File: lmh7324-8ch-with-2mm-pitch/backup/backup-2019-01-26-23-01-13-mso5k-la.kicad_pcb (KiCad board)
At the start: 4 copper layers, 40 x 44 mm, 101 parts, among them IC201 lmh7324, IC401 lmh7324, J101 out, J102 in, J103 3mm, J104 3mm, J105 3mm, J106 3mm, U401 ATtiny85-20SU

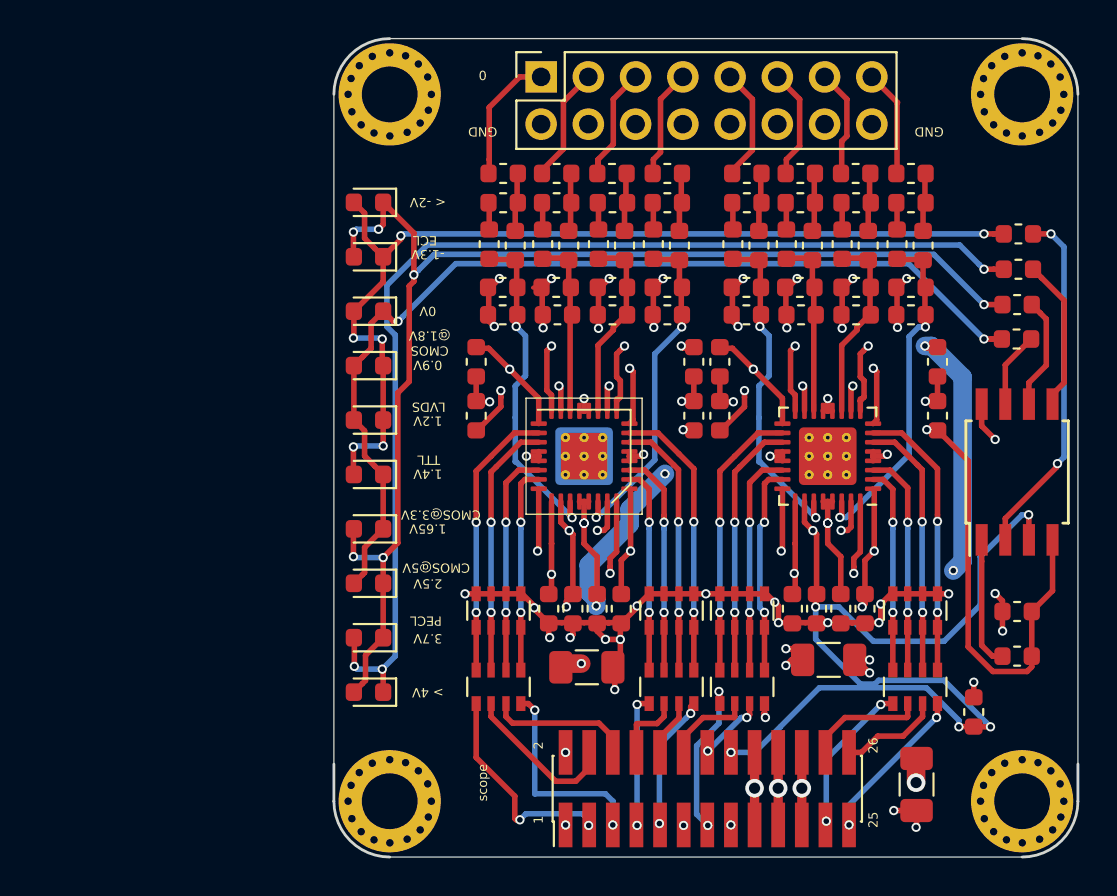
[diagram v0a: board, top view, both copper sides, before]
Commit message: Switched to an SMD 1.27 mm pitch header for the cable to the scope to get a thinner uplink ribbon
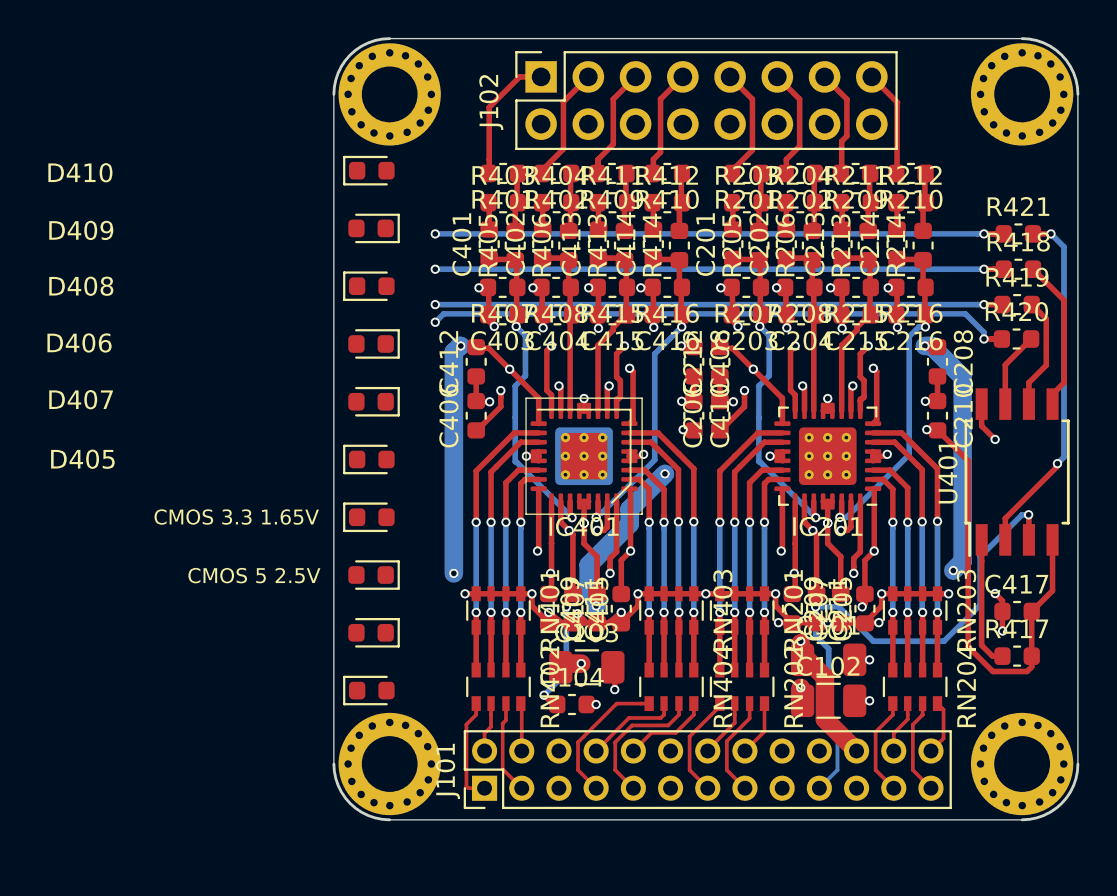
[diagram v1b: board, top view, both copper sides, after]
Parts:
- J101: footprint Connector_PinHeader_1.27mm:PinHeader_2x13_P1.27mm_Vertical_SMD -> Connector_PinHeader_2.00mm:PinHeader_2x13_P2.00mm_Vertical
- moved C104 21.6 mm to (57.8, 180.8), turned to 0 degrees
- moved J101 12.0 mm to (53.1, 185.3)
- moved C102 6.53 mm to (71.6, 180.6), turned to 0 degrees
- moved D406 4.09 mm to (47.0, 161.4)
- moved J104 2.00 mm to (48.0, 184.0)
- moved J106 2.00 mm to (82.0, 184.0)
- moved D407 1.95 mm to (47.0, 164.5)
- moved D410 1.71 mm to (47.0, 152.1), turned to 0 degrees
- moved D409 1.53 mm to (47.0, 155.2)
- moved D408 1.36 mm to (47.0, 158.3), turned to 0 degrees
- moved D405 0.82 mm to (47.0, 167.6), turned to 0 degrees
- moved D404 0.65 mm to (47.0, 170.7), turned to 0 degrees
- moved D403 0.47 mm to (47.0, 173.8)
- moved D402 0.30 mm to (47.0, 176.9)
- moved D401 0.20 mm to (47.0, 180.1), turned to 0 degrees
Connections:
- J101 pad 1: GND -> D1-
- J101 pad 10: D2+ -> D2-
- J101 pad 11: D4- -> GND
- J101 pad 12: D5+ -> GND
- J101 pad 14: D4+ -> D5+
- J101 pad 15: GND -> D4+
- J101 pad 16: Vref -> D4-
- J101 pad 17: -2V5 -> GND
- J101 pad 19: +2V5 -> Vref
- J101 pad 2: GND -> D1+
- J101 pad 21: +4V -> GND
- J101 pad 25: D6- -> D6+
- J101 pad 26: D6+ -> D6-
- J101 pad 3: D1- -> D0+
- J101 pad 4: D1+ -> D0-
- J101 pad 5: D0- -> GND
- J101 pad 6: D0+ -> GND
- J101 pad 9: D2- -> D2+
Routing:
- net Net-(D401-Pad2): track 69.0 -> 30.5 mm, vias 6 -> 2
- net Net-(D401-Pad1): track 60.1 -> 30.6 mm, vias 3 -> 2
- net Net-(D405-Pad2): track 53.0 -> 30.6 mm, vias 6 -> 2
- net Net-(D403-Pad2): track 53.0 -> 31.4 mm
- net GND: track 272.3 -> 290.5 mm, vias 43 -> 37
- net +2V5: track 155.2 -> 139.6 mm, vias 14 -> 13
- net +4V: track 108.2 -> 123.6 mm
- net Vref: track 144.4 -> 131.5 mm, vias 16 -> 14
- net D0-: track 12.3 -> 2.57 mm, vias 2 -> 0
- net -2V5: track 127.7 -> 120.9 mm, vias 16 -> 15
- net D1-: track 11.9 -> 5.68 mm, vias 2 -> 0
- net D4-: track 9.16 -> 2.98 mm, vias 2 -> 0
- net D6-: track 8.81 -> 2.96 mm, vias 2 -> 0
- net D1+: track 8.54 -> 2.69 mm
- net D2+: track 3.05 -> 7.51 mm
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- removed copper zone on 3_Misc, net +4V
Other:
- board size 40 x 44 mm -> 40 x 42 mm
- board text removed: "-1.3V"
- board text removed: "0"
- board text removed: "0.9V"
- board text removed: "0V"
- board text removed: "1"
- board text removed: "1.2V"
- board text removed: "1.4V"
- board text removed: "1.65V"
- board text removed: "2"
- board text removed: "2.5V"
- board text removed: "25"
- board text removed: "26"
- board text removed: "3.7V"
- board text removed: "< -2V"
- board text removed: "> 4V"
- board text removed: "CMOS @1.8V"
- board text removed: "CMOS@3.3V"
- board text removed: "CMOS@5V"
- board text removed: "ECL"
- board text removed: "GND"
- board text removed: "LVDS"
- board text removed: "PECL"
- board text removed: "TTL"
- board text removed: "scope"
